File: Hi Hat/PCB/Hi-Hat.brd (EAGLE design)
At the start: 100 x 50 mm, 91 parts, among them IC1 LM741P, IC2 LM741P, IC3 LM741P, IC4 LM741P, IC5 LM741P, IC6 LM741P, IC7 LM741P, Q1 2N2222A, Q6 2N3904, Q7 2N3904

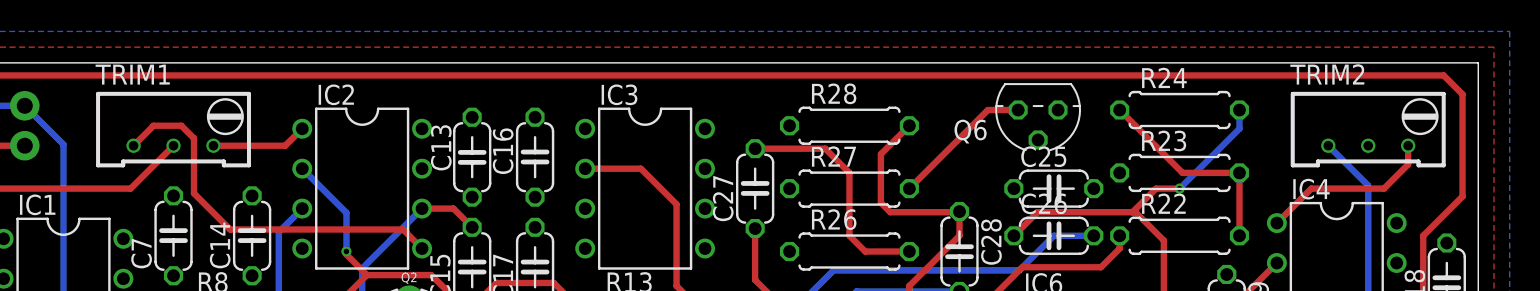
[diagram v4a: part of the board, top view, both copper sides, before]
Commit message: Worked on Hi-hat and waveform generator board
Changed trimpots to the proper part. Added test points to the waveform generator board and fixed silkscreen, ran DRC.
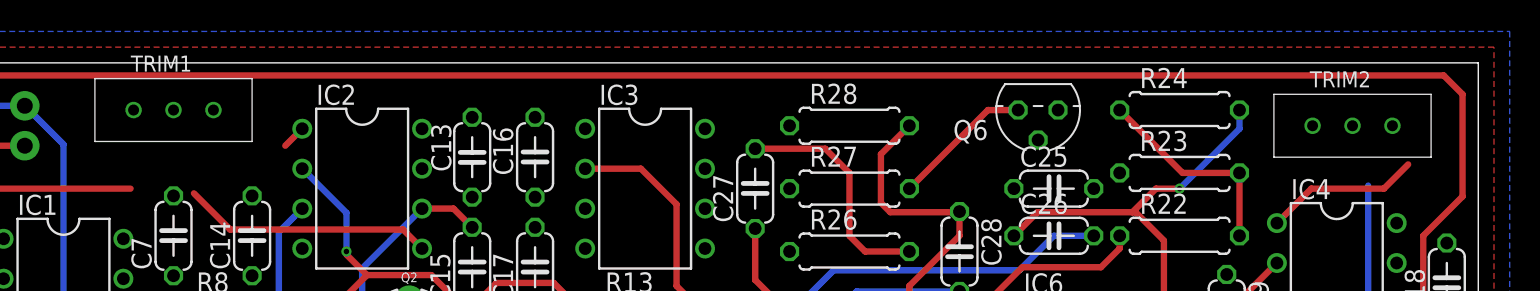
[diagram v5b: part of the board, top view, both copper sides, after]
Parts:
- TRIM1, TRIM2: device rcl:RTRIM64W -> Capstone:10K_TRIM
- moved TRIM2 6.32 mm to (87.0, 44.0), turned to 0 degrees
- moved TRIM1 5.10 mm to (12.0, 45.0), turned to 0 degrees
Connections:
- net -12V: now also TRIM1.P$2, TRIM2.P$2; no longer TRIM1.2, TRIM2.2
- net N$4: now also TRIM1.P$1; no longer TRIM1.1
- net N$67: now also TRIM2.P$1; no longer TRIM2.1
- net N$68: now also TRIM2.P$3; no longer TRIM2.3
- net N$7: now also TRIM1.P$3; no longer TRIM1.3
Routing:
- net N$4: track 24.2 -> 16.0 mm
- net N$7: track 6.10 -> 1.53 mm
- net -12V: track 29.8 -> 25.9 mm
- net N$67: track 14.3 -> 10.7 mm
- net N$68: track 11.1 -> 9.90 mm
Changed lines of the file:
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@@
 <attribute name="VALUE" x="100.667" y="33.841" size="1.27" layer="27" ratio="10" rot="R90"/>
-</element>
-<element name="TRIM2" library="rcl" library_urn="urn:adsk.eagle:library:334" package="RTRIM64W" package3d_urn="urn:adsk.eagle:package:23748/1" value="10k" x="93" y="46" smashed="yes" rot="R270">
-<attribute name="NAME" x="88.05" y="48.62" size="1.27" layer="25"/>
-<attribute name="SPICEMODEL" value="X" x="71" y="56" size="1.778" layer="27" rot="R270" display="off"/>
-<attribute name="SPICEPREFIXL" value="POT" x="71" y="56" size="1.778" layer="27" rot="R270" display="off"/>
-<attribute name="VALUE" x="88.05" y="41.65" size="1.27" layer="27"/>
 </element>
 <element name="Q5" library="Capstone" package="TO-92" value="" x="86" y="27" smashed="yes">
@@
 <attribute name="VALUE" x="33.333" y="46.159" size="1.27" layer="27" ratio="10" rot="R270"/>
 </element>
-<element name="TRIM1" library="rcl" library_urn="urn:adsk.eagle:library:334" package="RTRIM64W" package3d_urn="urn:adsk.eagle:package:23748/1" value="10k" x="17" y="46" smashed="yes" rot="R270">
-<attribute name="NAME" x="12.05" y="48.62" size="1.27" layer="25"/>
-<attribute name="SPICEMODEL" value="X" x="-1124" y="103" size="1.778" layer="27" rot="R270" display="off"/>
-<attribute name="SPICEPREFIXL" value="POT" x="-1124" y="103" size="1.778" layer="27" rot="R270" display="off"/>
-<attribute name="VALUE" x="12.05" y="41.65" size="1.27" layer="27"/>
-</element>
 <element name="Q3" library="Capstone" package="TO-92" value="" x="32" y="29" smashed="yes" rot="R180">
 <attribute name="NAME" x="32" y="25.952" size="0.6096" layer="25" font="vector" ratio="20" rot="R180" align="bottom-center"/>
@@
 <attribute name="SPICEPREFIX" value="R" x="60" y="42" size="1.778" layer="27" display="off"/>
 <attribute name="VALUE" x="57.714" y="41.4412" size="1.27" layer="27" ratio="10"/>
+</element>
+<element name="TRIM1" library="Capstone" package="10K_TRIM" value="10k" x="12" y="45" smashed="yes">
+<attribute name="NAME" x="14.286" y="49.445" size="1.016" layer="25"/>
+</element>
+<element name="TRIM2" library="Capstone" package="10K_TRIM" value="10k" x="87" y="44" smashed="yes">
+<attribute name="NAME" x="89.286" y="48.445" size="1.016" layer="25"/>
 </element>
 </elements>
@@
 <contactref element="C19" pad="2"/>
 <contactref element="IC4" pad="4"/>
-<contactref element="TRIM2" pad="2"/>
 <contactref element="R28" pad="1"/>
 <contactref element="R32" pad="1"/>
@@
 <contactref element="C14" pad="2"/>
 <contactref element="IC2" pad="4"/>
-<contactref element="TRIM1" pad="2"/>
 <contactref element="C17" pad="2"/>
 <contactref element="IC3" pad="4"/>
@@
 <contactref element="IC7" pad="4"/>
 <wire x1="3" y1="39.54" x2="5.46" y2="42" width="0.4064" layer="1"/>
-<wire x1="14.27" y1="42" x2="17" y2="44.73" width="0.4064" layer="1"/>
 <wire x1="5.46" y1="42" x2="14.27" y2="42" width="0.4064" layer="1"/>
 <wire x1="3" y1="39.54" x2="3" y2="37" width="0.4064" layer="1"/>
@@
 <wire x1="85" y1="4.46" x2="86.92" y2="4.46" width="0.4064" layer="1"/>
 <wire x1="86.92" y1="4.46" x2="88.19" y2="3.19" width="0.4064" layer="1"/>
-<wire x1="87.19" y1="32.19" x2="93" y2="44.73" width="0" layer="19" extent="1-1"/>
+<contactref element="TRIM1" pad="P$2"/>
+<contactref element="TRIM2" pad="P$2"/>
 <wire x1="84" y1="31.46" x2="87.19" y2="32.19" width="0" layer="19" extent="1-1"/>
 <wire x1="70.19" y1="26.19" x2="84" y2="31.46" width="0" layer="19" extent="1-1"/>
@@
 <wire x1="25.19" y1="38.19" x2="40" y2="39.54" width="0" layer="19" extent="1-1"/>
 <wire x1="22" y1="41.54" x2="25.19" y2="38.19" width="0" layer="19" extent="1-1"/>
-<wire x1="17" y1="44.73" x2="22" y2="41.54" width="0" layer="19" extent="1-1"/>
+<wire x1="14.27" y1="42" x2="22" y2="41.54" width="0" layer="19" extent="1-1"/>
 <wire x1="56.19" y1="46" x2="43.19" y2="38.19" width="0" layer="19" extent="1-1"/>
 <wire x1="20.19" y1="14" x2="6.19" y2="31.19" width="0" layer="19" extent="1-1"/>
 <wire x1="22.19" y1="6" x2="20.19" y2="14" width="0" layer="19" extent="1-1"/>
+<wire x1="17" y1="47" x2="22.19" y2="6" width="0" layer="19" extent="1-1"/>
+<wire x1="92" y1="46" x2="17" y2="47" width="0" layer="19" extent="1-1"/>
 </signal>
 <signal name="OUTPUT">
@@
 <signal name="N$67">
 <contactref element="IC4" pad="5"/>
-<contactref element="TRIM2" pad="1"/>
-<wire x1="90.46" y1="44.73" x2="93" y2="42.19" width="0.4064" layer="16"/>
 <wire x1="93" y1="34" x2="94.81" y2="32.19" width="0.4064" layer="16"/>
 <wire x1="93" y1="42.19" x2="93" y2="34" width="0.4064" layer="16"/>
+<contactref element="TRIM2" pad="P$1"/>
+<wire x1="89.46" y1="46" x2="93" y2="34" width="0" layer="19" extent="16-16"/>
 </signal>
 <signal name="N$68">
 <contactref element="IC4" pad="1"/>
-<contactref element="TRIM2" pad="3"/>
 <wire x1="87.19" y1="39.81" x2="89.38" y2="42" width="0.4064" layer="1"/>
 <wire x1="89.38" y1="42" x2="94" y2="42" width="0.4064" layer="1"/>
 <wire x1="94" y1="42" x2="95.54" y2="43.54" width="0.4064" layer="1"/>
-<wire x1="95.54" y1="43.54" x2="95.54" y2="44.73" width="0.4064" layer="1"/>
+<contactref element="TRIM2" pad="P$3"/>
+<wire x1="94.54" y1="46" x2="87.19" y2="39.81" width="0" layer="19" extent="1-1"/>
 </signal>
 <signal name="N$60">
@@
 <signal name="N$4">
 <contactref element="IC2" pad="5"/>
-<contactref element="TRIM1" pad="1"/>
-<wire x1="14.46" y1="44.73" x2="15.73" y2="46" width="0.4064" layer="1"/>
-<wire x1="17.5" y1="46" x2="18.3" y2="45.2" width="0.4064" layer="1"/>
-<wire x1="18.3" y1="45.2" x2="18.3" y2="41.7" width="0.4064" layer="1"/>
 <wire x1="31.6" y1="39.4" x2="32.81" y2="38.19" width="0.4064" layer="1"/>
-<wire x1="15.73" y1="46" x2="17.5" y2="46" width="0.4064" layer="1"/>
 <wire x1="18.3" y1="41.7" x2="20.6" y2="39.4" width="0.4064" layer="1"/>
 <wire x1="20.6" y1="39.4" x2="31.6" y2="39.4" width="0.4064" layer="1"/>
+<contactref element="TRIM1" pad="P$1"/>
+<wire x1="14.46" y1="47" x2="18.3" y2="41.7" width="0" layer="19" extent="1-1"/>
 </signal>
 <signal name="N$7">
 <contactref element="IC2" pad="1"/>
-<contactref element="TRIM1" pad="3"/>
-<wire x1="19.54" y1="44.73" x2="24.11" y2="44.73" width="0.4064" layer="1"/>
 <wire x1="24.11" y1="44.73" x2="25.19" y2="45.81" width="0.4064" layer="1"/>
+<contactref element="TRIM1" pad="P$3"/>
+<wire x1="19.54" y1="47" x2="24.11" y2="44.73" width="0" layer="19" extent="1-1"/>
 </signal>
 <signal name="N$8">

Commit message: Worked more on cymbals
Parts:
- added R12: 22k, rcl:0207/7
- moved IC1 2.00 mm to (10.0, 37.0)
- moved R1 2.00 mm to (5.00, 30.0)
- moved R2 2.00 mm to (5.00, 26.0)
- moved R3 2.00 mm to (5.00, 22.0)
- moved R4 2.00 mm to (5.00, 18.0)
- moved R5 2.00 mm to (5.00, 14.0)
- moved R6 2.00 mm to (5.00, 10.0)
- moved R7 2.00 mm to (5.00, 6.00)
- moved C8 1.00 mm to (3.00, 36.0), turned to 270 degrees
- moved C11 0.40 mm to (13.4, 2.00)
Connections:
- new net N$6: C11.2, C12.+, D1.C, R12.2, R6.2
- net POT2A: now also R12.1; no longer C11.2, C12.+, D1.C, R6.2
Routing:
- net -12V: track 25.9 -> 270.4 mm, vias 0 -> 7
- net POT1B: track 0.00 -> 63.2 mm, vias 0 -> 2
- net POT1A: track 5.16 -> 42.0 mm
- net N$72: track 13.3 -> 41.2 mm, vias 0 -> 1
- net N$6: track 0.00 -> 25.0 mm
- net PRE_CC: track 0.00 -> 23.8 mm
- net N$10: track 13.3 -> 31.1 mm, vias 0 -> 1
- net N$63: track 18.6 -> 32.7 mm
- net N$39: track 16.9 -> 29.1 mm
- net N$74: track 14.9 -> 27.1 mm
- net N$33: track 0.00 -> 10.1 mm
- net N$4: track 16.0 -> 25.9 mm
- net N$75: track 18.8 -> 28.3 mm
- net OUTPUT: track 14.3 -> 22.9 mm
- net POT2A: track 61.2 -> 66.6 mm
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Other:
- board text added: "SQ"
- board text added: "WN"

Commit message: Generated Gerbers
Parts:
- flipped D3 to the top
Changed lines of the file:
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@@
 <?xml version="1.0" encoding="utf-8"?>
 <!DOCTYPE eagle SYSTEM "eagle.dtd">
-<eagle version="9.3.0">
+<eagle version="9.2.2">
 <drawing>
 <settings>
@@
 <attribute name="VALUE" x="41.143" y="28" size="0.6096" layer="27" font="vector" ratio="20" rot="R90" align="top-center"/>
 </element>
-<element name="D3" library="SparkFun-DiscreteSemi" package="DIODE-1N4148" value="200mA/100V/1V" x="37" y="28" smashed="yes" rot="MR270">
-<attribute name="NAME" x="35.857" y="28" size="0.6096" layer="26" font="vector" ratio="20" rot="MR270" align="bottom-center"/>
-<attribute name="PROD_ID" value="DIO-08378" x="37" y="28" size="1.778" layer="28" rot="MR270" display="off"/>
-<attribute name="VALUE" x="38.143" y="28" size="0.6096" layer="28" font="vector" ratio="20" rot="MR270" align="top-center"/>
+<element name="D3" library="SparkFun-DiscreteSemi" package="DIODE-1N4148" value="200mA/100V/1V" x="37" y="28" smashed="yes" rot="R270">
+<attribute name="NAME" x="35.143" y="28" size="0.6096" layer="25" font="vector" ratio="20" rot="R270" align="bottom-center"/>
+<attribute name="PROD_ID" value="DIO-08378" x="37" y="28" size="1.778" layer="27" rot="R270" display="off"/>
+<attribute name="VALUE" x="35.857" y="28" size="0.6096" layer="27" font="vector" ratio="20" rot="R270" align="top-center"/>
 </element>
 <element name="D5" library="SparkFun-DiscreteSemi" package="DIODE-1N4148" value="200mA/100V/1V" x="81" y="17" smashed="yes" rot="R270">
@@
 <contactref element="D2" pad="A"/>
 <contactref element="D3" pad="C"/>
-<wire x1="40" y1="24.19" x2="37" y2="24.19" width="0.4064" layer="1"/>
+<wire x1="40" y1="24.19" x2="37" y2="24.19" width="0.4064" layer="16"/>
 <wire x1="40" y1="24.19" x2="46.19" y2="24.19" width="0.4064" layer="1"/>
 <wire x1="50.81" y1="28.81" x2="50.81" y2="30" width="0.4064" layer="1"/>
@@
 <contactref element="D3" pad="A"/>
 <contactref element="R22" pad="1"/>
-<wire x1="37" y1="31.81" x2="40" y2="31.81" width="0.4064" layer="1"/>
+<wire x1="37" y1="31.81" x2="40" y2="31.81" width="0.4064" layer="16"/>
 <wire x1="40" y1="31.81" x2="63.81" y2="31.81" width="0.4064" layer="1"/>
 <wire x1="63.81" y1="31.81" x2="66" y2="34" width="0.4064" layer="1"/>
